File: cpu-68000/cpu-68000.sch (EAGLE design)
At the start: 105 parts, among them IC201 AS6C4008, IC202 AS6C4008, IC203 39SF040, IC204 39SF040, IC301 XR68C681, IC302 DS1244Y, IC303 MAX232, IC401 GAL22V10, IC402 GAL22V10, IC403 74HC14D, IC404 LM3724, IC405 74HC175D, J201 POWER_JACK, Q301 3.6864 MHz

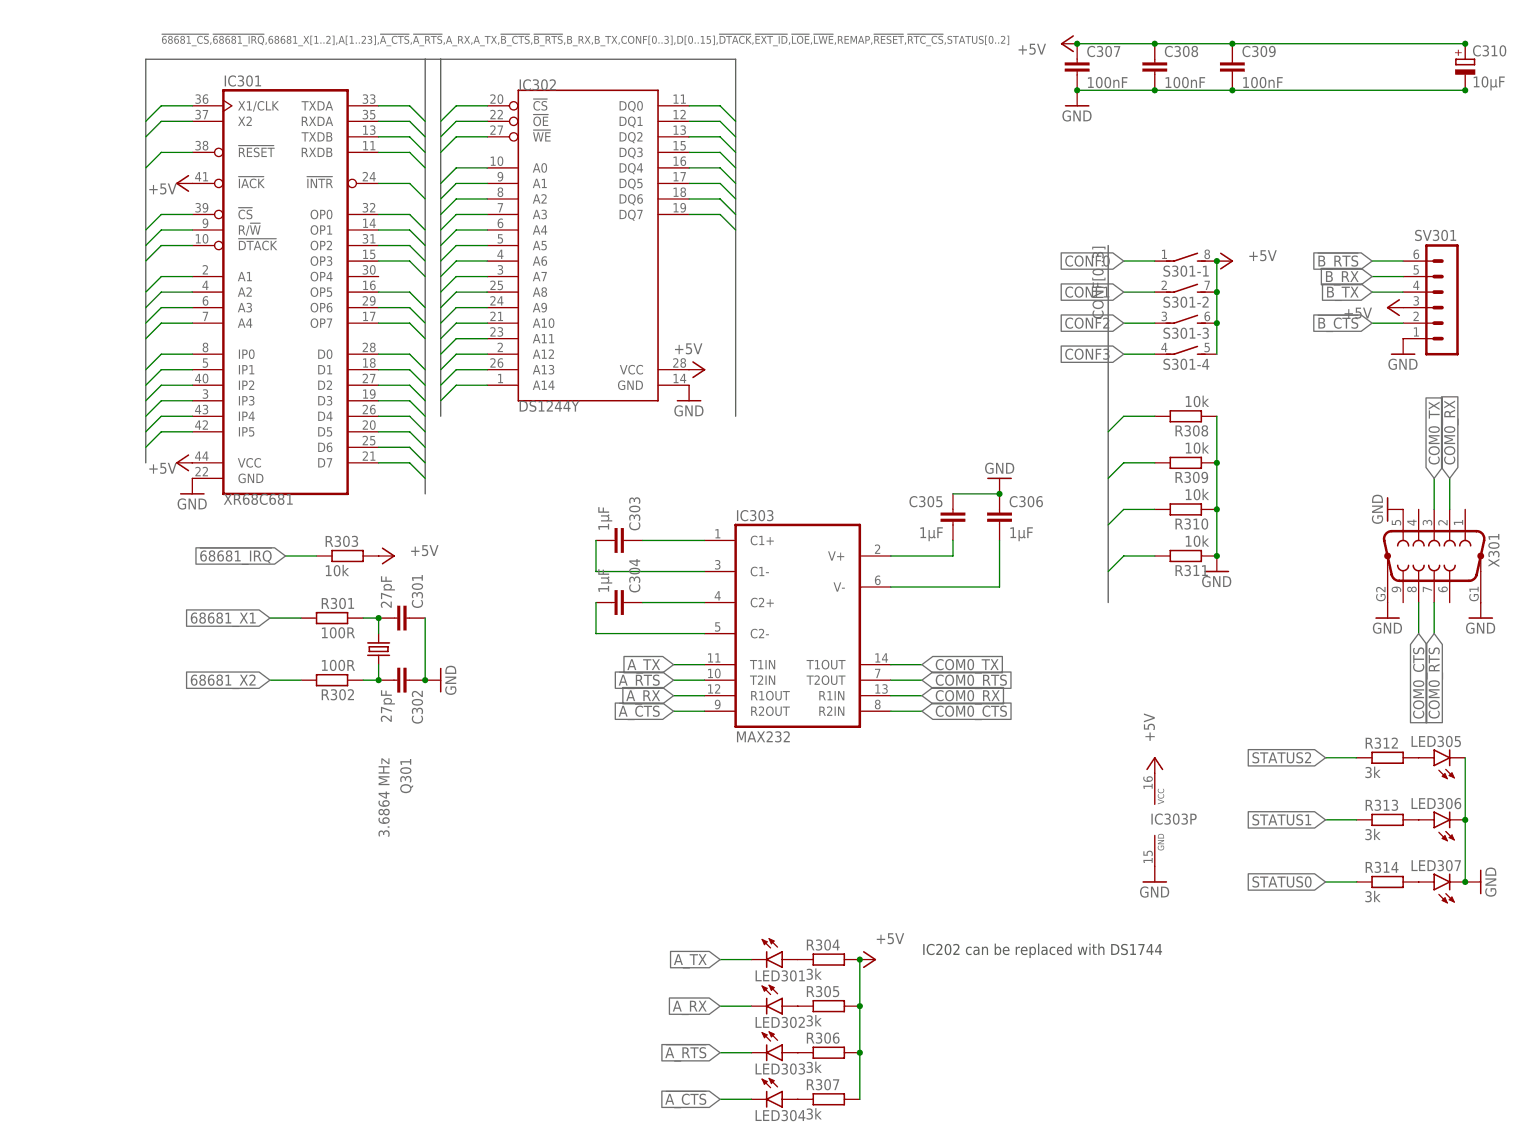
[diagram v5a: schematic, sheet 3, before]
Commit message: Rev01 of CPU-68000 and 2MB SRAM board sent to production
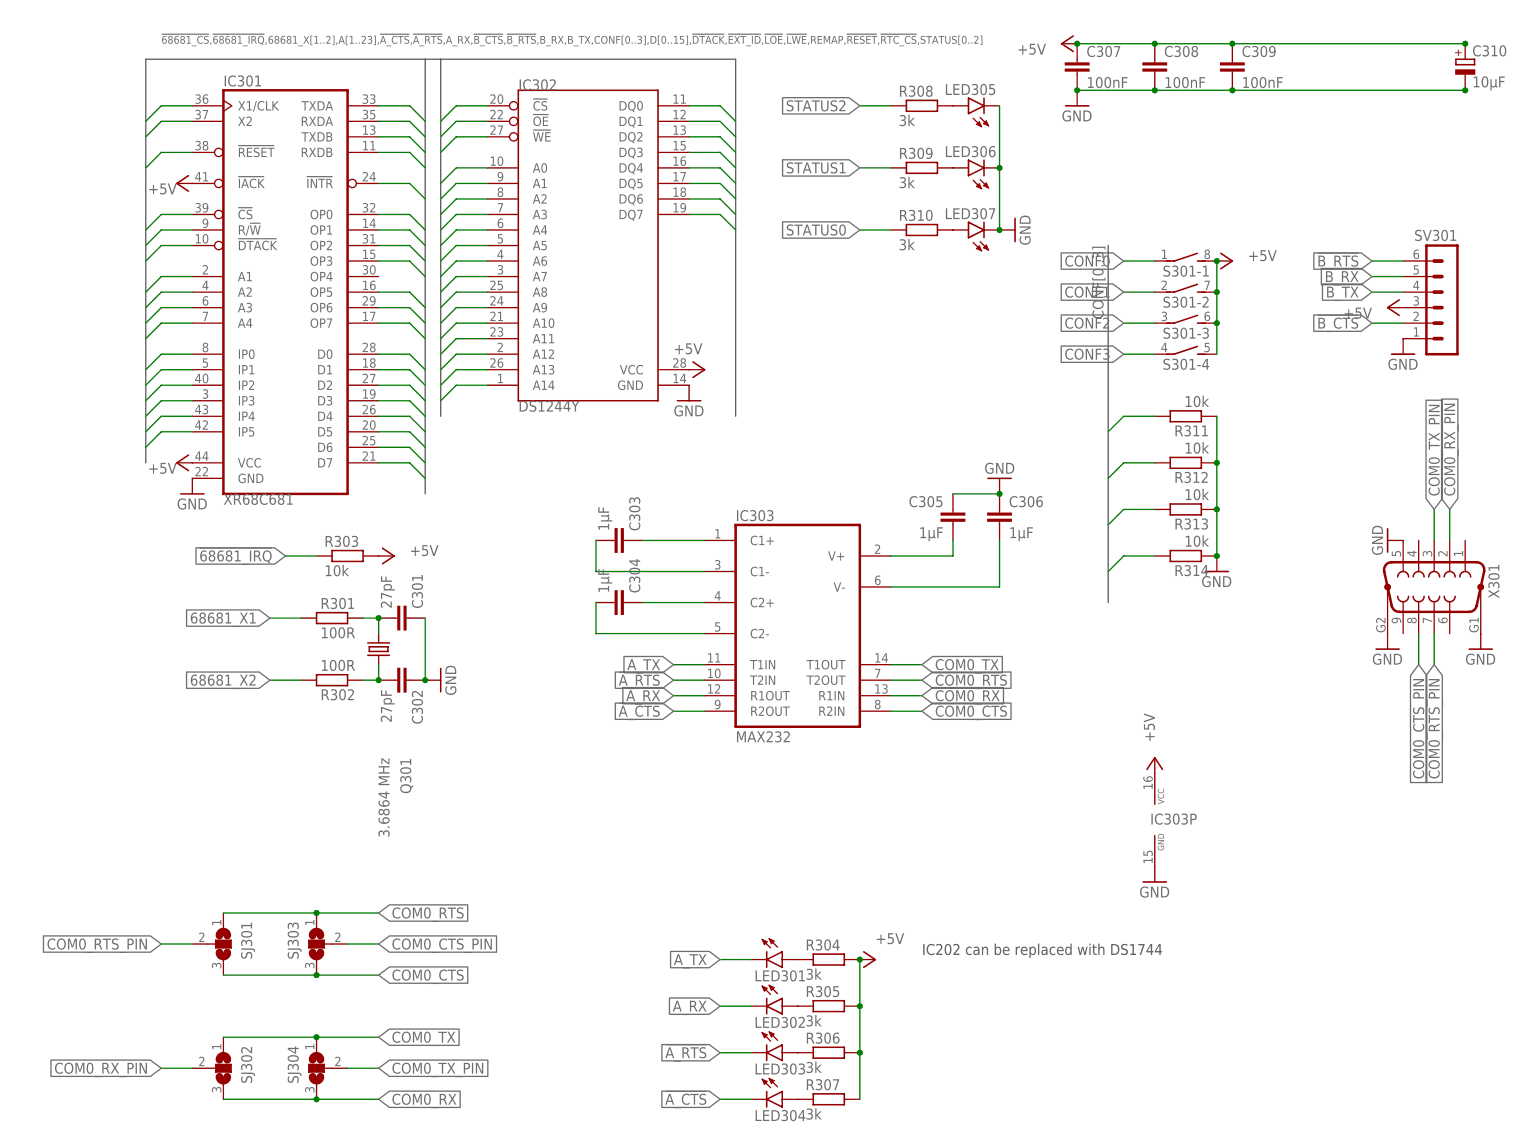
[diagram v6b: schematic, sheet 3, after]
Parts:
- removed C1: 1µF, rcl:C-EUC0805
- added C106: 10µF, rcl:CPOL-EUSMCB
- added LED101, LED102: (no value), led:LEDCHIPLED_1206
- added R121, R122: 10k, rcl:R-EU_R2012
- added SJ301, SJ302, SJ303, SJ304: (no value), jumper:SJ2WW
- C102: value 100nF -> 1µF; MOUSER 710-885012207072 -> 710-885012207078
- C104: value 10µF -> 100nF; device rcl:CPOL-EUSMCB -> rcl:C-EUC0805; MOUSER 581-TAJB106K020RNJV -> 710-885012207072
- R101, R102, R308, R309, R310: value 10k -> 3k; MOUSER 652-CR0805FX-1002ELF -> 652-CR0805JW-302ELF
- R312, R313, R314: value 3k -> 10k; MOUSER 652-CR0805JW-302ELF -> 652-CR0805FX-1002ELF
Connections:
- new net COM0_CTS_PIN: SJ303.2, X301.8
- new net COM0_RTS_PIN: SJ301.2, X301.7
- new net COM0_RX_PIN: SJ302.2, X301.2
- new net COM0_TX_PIN: SJ304.2, X301.3
- new net N$18: LED101.A, R101.1
- new net N$19: LED102.A, R102.1
- net !BR: now also R106.1; no longer R104.1
- net !DTACK: now also R103.1; no longer R101.1
- net !HALT: now also LED102.C, R105.1; no longer R103.1
- net !RESET: now also LED101.C, R104.1; no longer R102.1
- net +5V: now also C104.1, C106.+, R105.2, R106.2; no longer C1.1, C104.+
- net COM0_CTS: now also SJ301.3, SJ303.3; no longer X301.8
- net COM0_RTS: now also SJ301.1, SJ303.1; no longer X301.7
- net COM0_RX: now also SJ302.3, SJ304.3; no longer X301.2
- net COM0_TX: now also SJ302.1, SJ304.1; no longer X301.3
- net CONF0: now also R311.2; no longer R308.2
- net CONF1: now also R312.2; no longer R309.2
- net CONF2: now also R313.2; no longer R310.2
- net CONF3: now also R314.2; no longer R311.2
- net D0: now also R107.2; no longer R105.2
- net D1: now also R108.2; no longer R106.2
- net D10: now also R117.2; no longer R115.2
- net D11: now also R118.2; no longer R116.2
- net D12: now also R119.2; no longer R117.2
- net D13: now also R120.2; no longer R118.2
- net D14: now also R121.2; no longer R119.2
- net D15: now also R122.2; no longer R120.2
- net D2: now also R109.2; no longer R107.2
- net D3: now also R110.2; no longer R108.2
- net D4: now also R111.2; no longer R109.2
- net D5: now also R112.2; no longer R110.2
- net D6: now also R113.2; no longer R111.2
- net D7: now also R114.2; no longer R112.2
- net D8: now also R115.2; no longer R113.2
- net D9: now also R116.2; no longer R114.2
- net GND: now also C104.2, C106.-, R121.1, R122.1, R312.1, R313.1, R314.1; no longer C1.2, C104.-, R105.1, R106.1, R308.1, R309.1, R310.1
- net N$10: now also R308.2; no longer R312.2
- net N$7: now also R309.2; no longer R313.2
- net N$9: now also R310.2; no longer R314.2
- net STATUS0: now also R310.1; no longer R314.1
- net STATUS1: now also R309.1; no longer R313.1
- net STATUS2: now also R308.1; no longer R312.1
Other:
- moved on the sheet: C101, C102, C103, C105, LED305, LED306, LED307, R101, R102, R103, R104, R105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
